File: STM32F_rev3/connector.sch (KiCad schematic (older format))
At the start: 26 parts, among them J3 502225-0801, Q5 2N3904, Q6 IRF540N, Q7 IRF540N, U4 MIC2940A-3.3WU, U5 MIC2940A-5.0WT, U6 LT4363IMS, U7 MIC2940A-5.0WT

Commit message: los espacios me dan ansiedad
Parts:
- J3: footprint OpenEFI-STM32F rev3:502225-0801 -> OpenEFI-STM32F_rev3:502225-0801
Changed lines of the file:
@@
 F 0 "J3" H 10428 -1097 60  0000 L CNN
 F 1 "502225-0801" H 10428 -1203 60  0000 L CNN
-F 2 "OpenEFI-STM32F rev3:502225-0801" H 10300 -1260 60  0001 C CNN
+F 2 "OpenEFI-STM32F_rev3:502225-0801" H 10300 -1260 60  0001 C CNN
 F 3 "" H 9900 800 60  0000 C CNN
 	1    9900 800
@@
 F 0 "J3" H 8578 -1097 60  0000 L CNN
 F 1 "502225-0801" H 8578 -1203 60  0000 L CNN
-F 2 "OpenEFI-STM32F rev3:502225-0801" H 8450 -1260 60  0001 C CNN
+F 2 "OpenEFI-STM32F_rev3:502225-0801" H 8450 -1260 60  0001 C CNN
 F 3 "" H 8050 800 60  0000 C CNN
 	2    8050 800

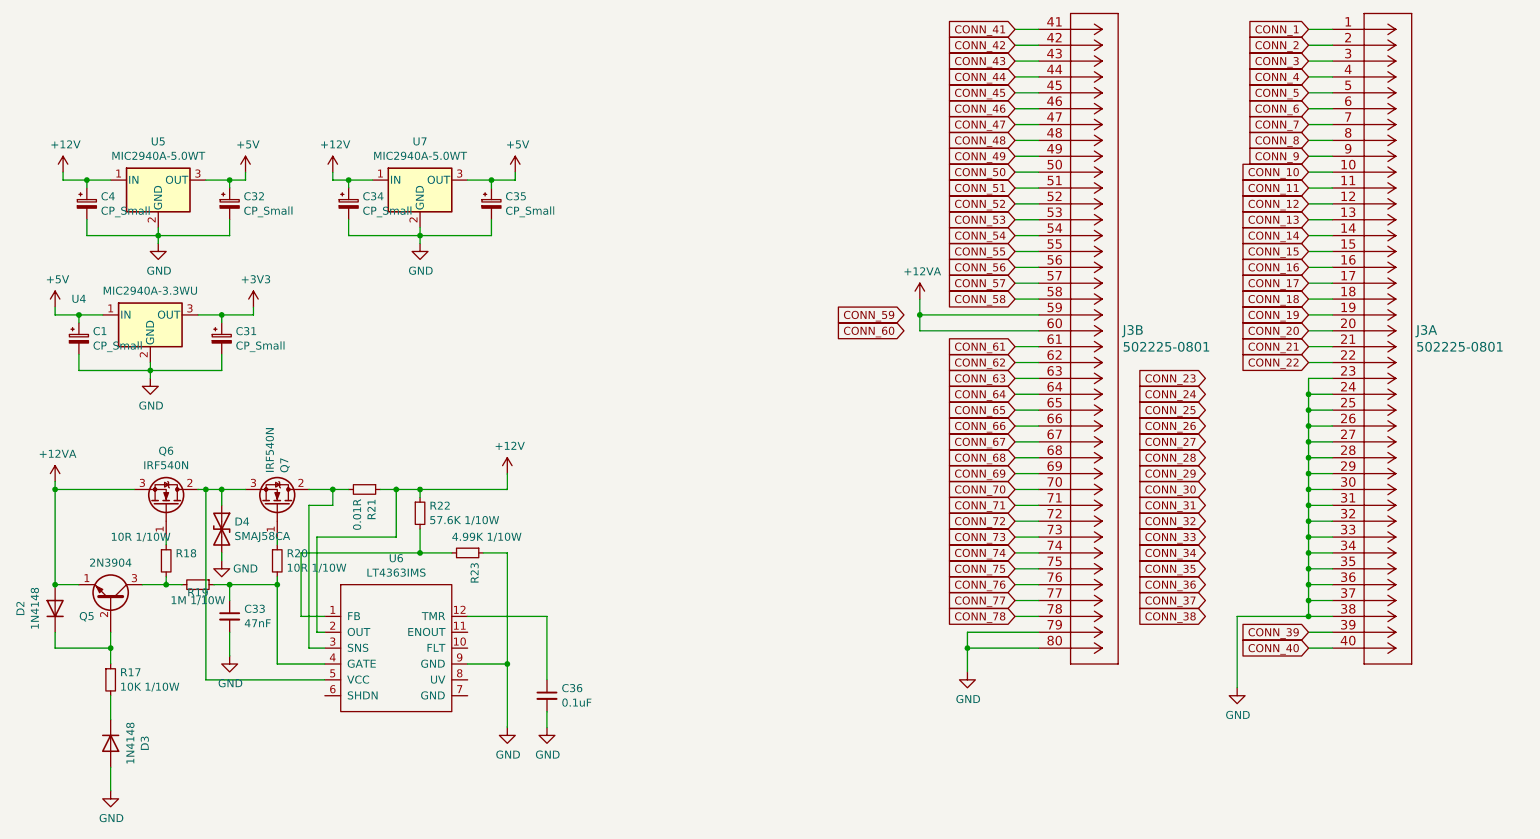
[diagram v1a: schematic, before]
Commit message: fix DRC error
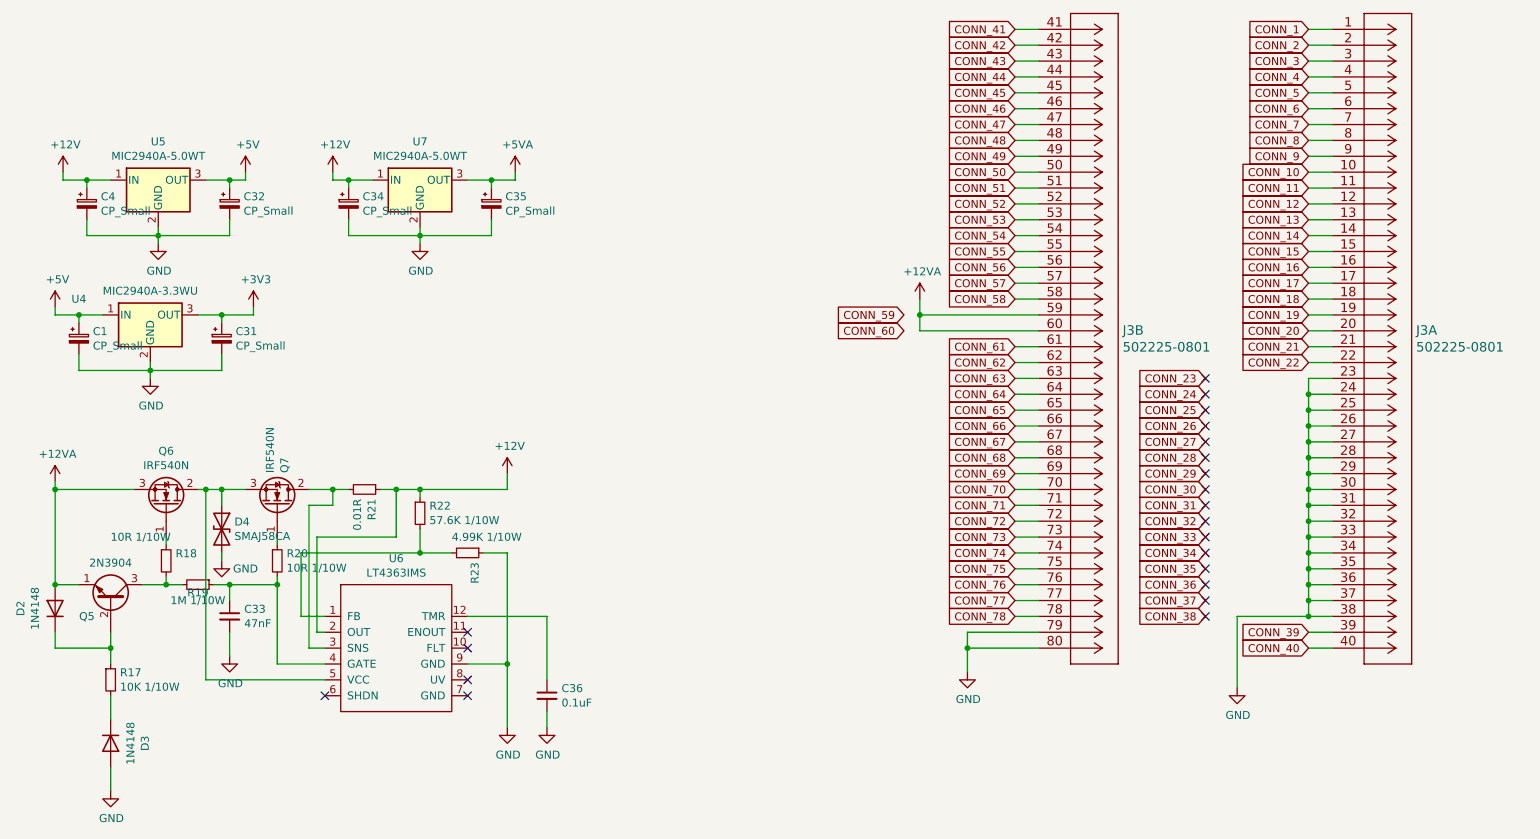
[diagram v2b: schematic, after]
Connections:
- net +5V: no longer C35.1, U7.3 (OUT)
- new net +5VA: C35.1, U7.3 (OUT)
- no-connect marks 0 -> 21
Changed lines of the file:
@@
-$EndComp
-$Comp
-L power:+5V #PWR023
-U 1 1 5FB3D647
-P 4750 1700
-F 0 "#PWR023" H 4750 1550 50  0001 C CNN
-F 1 "+5V" H 4765 1873 50  0000 C CNN
-F 2 "" H 4750 1700 50  0001 C CNN
-F 3 "" H 4750 1700 50  0001 C CNN
-	1    4750 1700
-	1    0    0    -1
 $EndComp
 $Comp
@@
 Wire Wire Line
 	9750 4300 9750 4400
+$Comp
+L power:+5VA #PWR0164
+U 1 1 5FAE216A
+P 4750 1700
+F 0 "#PWR0164" H 4750 1550 50  0001 C CNN
+F 1 "+5VA" H 4765 1873 50  0000 C CNN
+F 2 "" H 4750 1700 50  0001 C CNN
+F 3 "" H 4750 1700 50  0001 C CNN
+	1    4750 1700
+	1    0    0    -1
+$EndComp
+NoConn ~ 9100 3000
+NoConn ~ 9100 3100
+NoConn ~ 9100 3200
+NoConn ~ 9100 3300
+NoConn ~ 9100 3400
+NoConn ~ 9100 3500
+NoConn ~ 9100 3600
+NoConn ~ 9100 3700
+NoConn ~ 9100 3800
+NoConn ~ 9100 3900
+NoConn ~ 9100 4000
+NoConn ~ 9100 4100
+NoConn ~ 9100 4200
+NoConn ~ 9100 4300
+NoConn ~ 9100 4400
+NoConn ~ 9100 4500
+NoConn ~ 4450 4600
+NoConn ~ 4450 4700
+NoConn ~ 4450 4900
+NoConn ~ 4450 5000
+NoConn ~ 3550 5000
 $EndSCHEMATC
